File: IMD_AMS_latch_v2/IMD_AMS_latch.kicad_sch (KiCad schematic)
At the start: 40 parts, among them J10 Conn_01x02, J11 Conn_01x02, J12 Conn_01x02, J2 Conn_01x02, J5 Conn_01x02, J6 Conn_01x02, J7 Conn_01x02, J8 Conn_01x02, J9 Conn_01x02, K1 SANYOU_SRD_Form_C, K2 SANYOU_SRD_Form_C, Q1 AO3400A, Q2 AO3400A, U1 MC14044BDR2G, U2 LM393

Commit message: added TS indicator
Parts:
- removed J11, J12: Conn_01x02, Connector_Molex:Molex_Micro-Fit_3.0_43650-0215_1x02_P3.00mm_Vertical, symbol Connector_Generic:Conn_01x02
- added D5, D6: LED, LED_SMD:LED_0805_2012Metric_Pad1.15x1.40mm_HandSolder, symbol Device:LED
- added J13: Conn_01x02, Connector_Molex:Molex_Micro-Fit_3.0_43650-0215_1x02_P3.00mm_Vertical, symbol Connector_Generic:Conn_01x02
- added R16, R17: R_US, Resistor_SMD:R_0805_2012Metric_Pad1.20x1.40mm_HandSolder, symbol Device:R_US
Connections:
- net +12V: now also R16.2, R17.2
- net GND: now also J13.2 (Pin_2)
- net at D1.2 (A), K1.5, Q1.3 (D): now also D5.1 (K)
- net at D4.2 (A), R10.2: now also J13.1 (Pin_1)
- net at D2.2 (A), K2.5, Q2.3 (D): now also D6.1 (K)
- new net: D5.2 (A), R16.1
- new net: D6.2 (A), R17.1
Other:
- note added: "external IMD led"

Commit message: changed to horizontal molex microfit
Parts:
- J10, J13, J2, J5, J6, J7, J8, J9: footprint Connector_Molex:Molex_Micro-Fit_3.0_43650-0215_1x02_P3.00mm_Vertical -> Connector_Molex:Molex_Micro-Fit_3.0_43650-0200_1x02_P3.00mm_Horizontal
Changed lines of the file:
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@@
 			)
 		)
-		(property "Footprint" "Connector_Molex:Molex_Micro-Fit_3.0_43650-0215_1x02_P3.00mm_Vertical"
+		(property "Footprint" "Connector_Molex:Molex_Micro-Fit_3.0_43650-0200_1x02_P3.00mm_Horizontal"
 			(at 182.88 135.89 0)
 			(effects
@@
 			)
 		)
-		(property "Footprint" "Connector_Molex:Molex_Micro-Fit_3.0_43650-0215_1x02_P3.00mm_Vertical"
+		(property "Footprint" "Connector_Molex:Molex_Micro-Fit_3.0_43650-0200_1x02_P3.00mm_Horizontal"
 			(at 256.54 147.32 0)
 			(effects
@@
 			)
 		)
-		(property "Footprint" "Connector_Molex:Molex_Micro-Fit_3.0_43650-0215_1x02_P3.00mm_Vertical"
+		(property "Footprint" "Connector_Molex:Molex_Micro-Fit_3.0_43650-0200_1x02_P3.00mm_Horizontal"
 			(at 64.77 128.27 0)
 			(effects
@@
 			)
 		)
-		(property "Footprint" "Connector_Molex:Molex_Micro-Fit_3.0_43650-0215_1x02_P3.00mm_Vertical"
+		(property "Footprint" "Connector_Molex:Molex_Micro-Fit_3.0_43650-0200_1x02_P3.00mm_Horizontal"
 			(at 213.36 132.08 0)
 			(effects
@@
 			)
 		)
-		(property "Footprint" "Connector_Molex:Molex_Micro-Fit_3.0_43650-0215_1x02_P3.00mm_Vertical"
+		(property "Footprint" "Connector_Molex:Molex_Micro-Fit_3.0_43650-0200_1x02_P3.00mm_Horizontal"
 			(at 57.15 152.4 0)
 			(effects
@@
 			)
 		)
-		(property "Footprint" "Connector_Molex:Molex_Micro-Fit_3.0_43650-0215_1x02_P3.00mm_Vertical"
+		(property "Footprint" "Connector_Molex:Molex_Micro-Fit_3.0_43650-0200_1x02_P3.00mm_Horizontal"
 			(at 60.96 175.26 0)
 			(effects
@@
 			)
 		)
-		(property "Footprint" "Connector_Molex:Molex_Micro-Fit_3.0_43650-0215_1x02_P3.00mm_Vertical"
+		(property "Footprint" "Connector_Molex:Molex_Micro-Fit_3.0_43650-0200_1x02_P3.00mm_Horizontal"
 			(at 158.75 148.59 0)
 			(effects
@@
 			)
 		)
-		(property "Footprint" "Connector_Molex:Molex_Micro-Fit_3.0_43650-0215_1x02_P3.00mm_Vertical"
+		(property "Footprint" "Connector_Molex:Molex_Micro-Fit_3.0_43650-0200_1x02_P3.00mm_Horizontal"
 			(at 57.15 147.32 0)
 			(effects

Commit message: minor update on SDC IN & SDC out wiring
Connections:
- net SDC_IN: now also J7.2 (Pin_2); no longer J7.1 (Pin_1)
- net SDC_OUT: now also J7.1 (Pin_1); no longer J7.2 (Pin_2)
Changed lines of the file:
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@@
+	(wire
+		(pts
+			(xy 39.37 175.26) (xy 55.88 175.26)
+		)
+		(stroke
+			(width 0)
+			(type default)
+		)
+	)
 	(wire
 		(pts
@@
 	(wire
 		(pts
-			(xy 45.72 177.8) (xy 55.88 177.8)
-		)
-		(stroke
-			(width 0)
-			(type default)
-		)
-	)
-	(wire
-		(pts
 			(xy 186.69 53.34) (xy 193.04 53.34)
 		)
@@
 	(wire
 		(pts
+			(xy 39.37 177.8) (xy 55.88 177.8)
+		)
+		(stroke
+			(width 0)
+			(type default)
+		)
+	)
+	(wire
+		(pts
 			(xy 199.39 39.37) (xy 193.04 39.37)
 		)
@@
 		(pts
 			(xy 69.85 93.98) (xy 69.85 97.79)
-		)
-		(stroke
-			(width 0)
-			(type default)
-		)
-	)
-	(wire
-		(pts
-			(xy 45.72 175.26) (xy 55.88 175.26)
 		)
 		(stroke
@@
 		)
 	)
+	(label "SDC_IN"
+		(at 39.37 177.8 0)
+		(effects
+			(font
+				(size 1.27 1.27)
+			)
+			(justify left bottom)
+		)
+	)
 	(label "IMD_KL31_GND"
 		(at 194.31 134.62 0)
@@
 		)
 	)
+	(label "SDC_OUT"
+		(at 39.37 175.26 0)
+		(effects
+			(font
+				(size 1.27 1.27)
+			)
+			(justify left bottom)
+		)
+	)
 	(label "AMS_latch"
 		(at 214.63 58.42 0)
@@
 		)
 	)
-	(label "SDC_OUT"
-		(at 45.72 177.8 0)
-		(effects
-			(font
-				(size 1.27 1.27)
-			)
-			(justify left bottom)
-		)
-	)
 	(label "AMS_reset"
 		(at 87.63 38.1 0)
@@
 		(effects
 			(font
-				(size 1.27 1.27)
-			)
-			(justify left bottom)
-		)
-	)
-	(label "SDC_IN"
-		(at 45.72 175.26 0)
-		(effects
-			(font

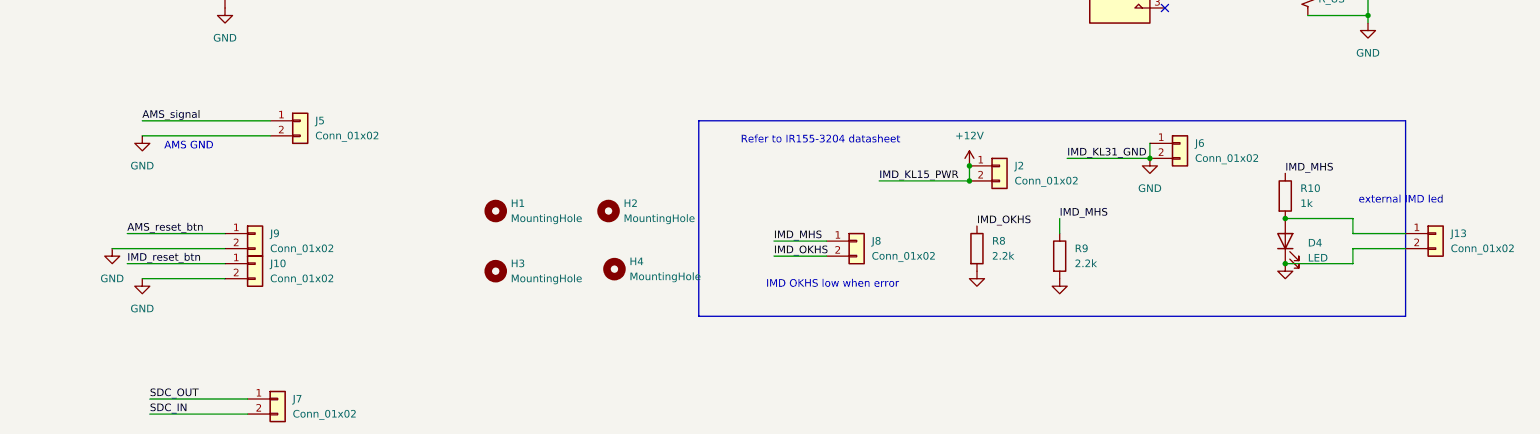
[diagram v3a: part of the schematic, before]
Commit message: fixed connectors
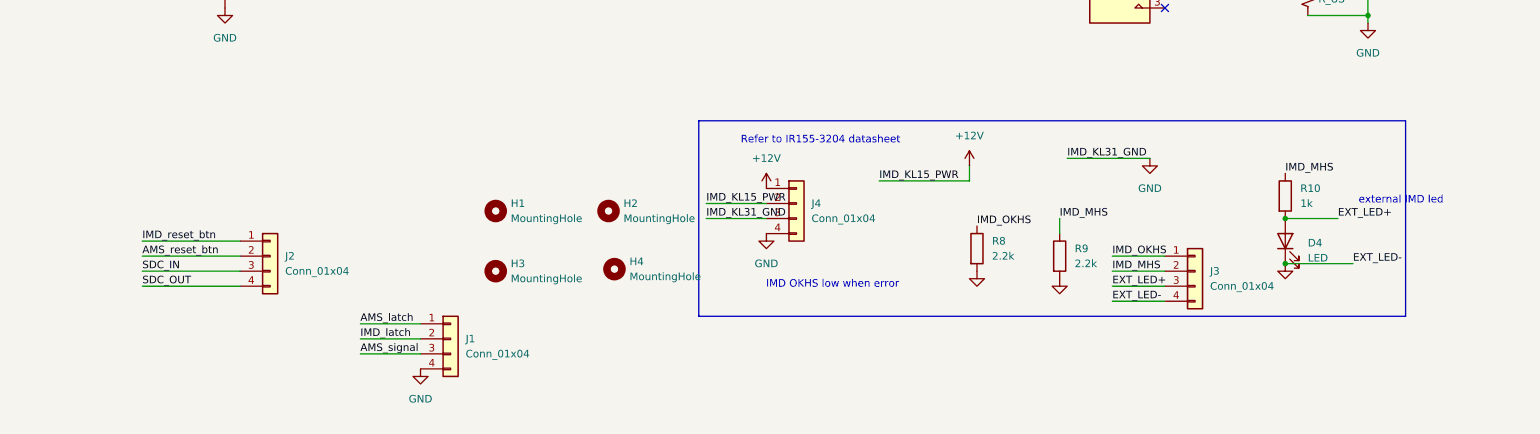
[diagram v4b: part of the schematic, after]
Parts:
- removed J10, J13, J2, J5, J6, J7, J8, J9: Conn_01x02, Connector_Molex:Molex_Micro-Fit_3.0_43650-0200_1x02_P3.00mm_Horizontal, symbol Connector_Generic:Conn_01x02
- added J1, J2, J3, J4: Conn_01x04, Connector_Molex:Molex_Micro-Fit_3.0_43045-0400_2x02_P3.00mm_Horizontal, symbol Connector_Generic:Conn_01x04
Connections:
- net +12V: now also J4.1 (Pin_1), J4.2 (Pin_2)
- net AMS_latch: now also J1.1 (Pin_1)
- net AMS_reset_btn: now also J2.2 (Pin_2)
- net AMS_signal: now also J1.3 (Pin_3)
- net GND: now also J1.4 (Pin_4), J3.4 (Pin_4), J4.3 (Pin_3), J4.4 (Pin_4)
- net IMD_MHS: now also J3.2 (Pin_2)
- net IMD_OKHS: now also J3.1 (Pin_1)
- net IMD_latch: now also J1.2 (Pin_2)
- net IMD_reset_btn: now also J2.1 (Pin_1)
- net SDC_IN: now also J2.3 (Pin_3)
- net SDC_OUT: now also J2.4 (Pin_4)
- net EXT_LED+: now reaches D4.2 (A), R10.2
- net EXT_LED+: now also J3.3 (Pin_3)
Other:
- note removed: "AMS GND"

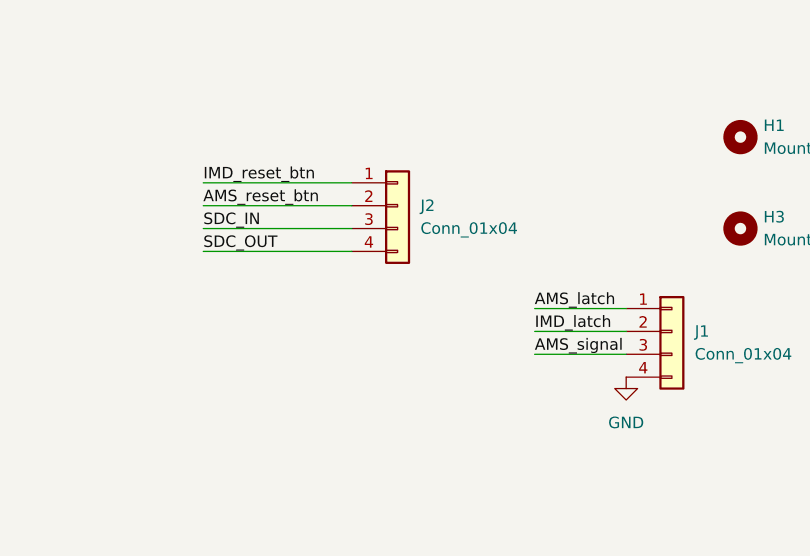
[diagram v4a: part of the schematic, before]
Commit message: fixed connectors
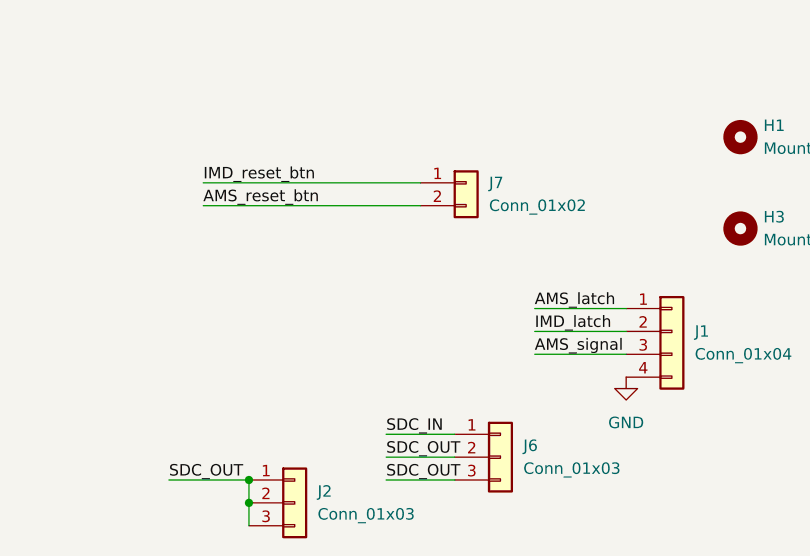
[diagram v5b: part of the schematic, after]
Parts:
- removed J2: Conn_01x04, Connector_Molex:Molex_Micro-Fit_3.0_43045-0400_2x02_P3.00mm_Horizontal, symbol Connector_Generic:Conn_01x04
- added J2, J6: Conn_01x03, Connector_Molex:Molex_Micro-Fit_3.0_43650-0300_1x03_P3.00mm_Horizontal, symbol Connector_Generic:Conn_01x03
- added J7: Conn_01x02, Connector_Molex:Molex_Micro-Fit_3.0_43650-0200_1x02_P3.00mm_Horizontal, symbol Connector_Generic:Conn_01x02
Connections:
- net AMS_reset_btn: now also J7.2 (Pin_2)
- net IMD_reset_btn: now also J7.1 (Pin_1)
- net SDC_IN: now also J6.1 (Pin_1)
- net SDC_OUT: now also J2.1 (Pin_1), J2.2 (Pin_2), J2.3 (Pin_3), J6.2 (Pin_2), J6.3 (Pin_3)
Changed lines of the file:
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@@
 	)
 	(junction
+		(at 43.18 184.15)
+		(diameter 0)
+		(color 0 0 0 0)
+	)
+	(junction
 		(at 215.9 96.52)
 		(diameter 0)
@@
 		(color 0 0 0 0)
 	)
+	(junction
+		(at 43.18 181.61)
+		(diameter 0)
+		(color 0 0 0 0)
+	)
 	(no_connect
 		(at 147.32 81.28)
@@
 	(wire
 		(pts
-			(xy 38.1 148.59) (xy 54.61 148.59)
+			(xy 38.1 148.59) (xy 62.23 148.59)
 		)
 		(stroke
@@
 	(wire
 		(pts
-			(xy 245.11 68.58) (xy 245.11 67.31)
+			(xy 58.42 181.61) (xy 66.04 181.61)
 		)
 		(stroke
@@
 	(wire
 		(pts
-			(xy 186.69 63.5) (xy 195.58 63.5)
+			(xy 245.11 68.58) (xy 245.11 67.31)
 		)
 		(stroke
@@
 	(wire
 		(pts
-			(xy 19.05 25.4) (xy 30.48 25.4)
+			(xy 186.69 63.5) (xy 195.58 63.5)
 		)
 		(stroke
@@
 	(wire
 		(pts
-			(xy 52.07 60.96) (xy 57.15 60.96)
+			(xy 19.05 25.4) (xy 30.48 25.4)
 		)
 		(stroke
@@
 	(wire
 		(pts
-			(xy 201.93 151.13) (xy 210.82 151.13)
+			(xy 52.07 60.96) (xy 57.15 60.96)
 		)
 		(stroke
@@
 	(wire
 		(pts
-			(xy 177.8 74.93) (xy 224.79 74.93)
+			(xy 201.93 151.13) (xy 210.82 151.13)
 		)
 		(stroke
@@
 	(wire
 		(pts
-			(xy 162.56 138.43) (xy 177.8 138.43)
+			(xy 177.8 74.93) (xy 224.79 74.93)
 		)
 		(stroke
@@
 	(wire
 		(pts
-			(xy 38.1 153.67) (xy 54.61 153.67)
+			(xy 162.56 138.43) (xy 177.8 138.43)
 		)
 		(stroke
@@
 	(wire
 		(pts
-			(xy 38.1 151.13) (xy 54.61 151.13)
+			(xy 43.18 181.61) (xy 43.18 184.15)
+		)
+		(stroke
+			(width 0)
+			(type default)
+		)
+	)
+	(wire
+		(pts
+			(xy 38.1 151.13) (xy 62.23 151.13)
 		)
 		(stroke
@@
 	(wire
 		(pts
+			(xy 58.42 176.53) (xy 66.04 176.53)
+		)
+		(stroke
+			(width 0)
+			(type default)
+		)
+	)
+	(wire
+		(pts
 			(xy 234.95 102.87) (xy 234.95 101.6)
 		)
@@
 	(wire
 		(pts
-			(xy 38.1 156.21) (xy 54.61 156.21)
+			(xy 199.39 39.37) (xy 193.04 39.37)
 		)
 		(stroke
@@
 	(wire
 		(pts
-			(xy 199.39 39.37) (xy 193.04 39.37)
+			(xy 40.64 76.2) (xy 40.64 74.93)
 		)
 		(stroke
@@
 	(wire
 		(pts
-			(xy 40.64 76.2) (xy 40.64 74.93)
+			(xy 69.85 93.98) (xy 69.85 97.79)
 		)
 		(stroke
@@
 	(wire
 		(pts
-			(xy 69.85 93.98) (xy 69.85 97.79)
+			(xy 147.32 35.56) (xy 147.32 36.83)
 		)
 		(stroke
@@
 	(wire
 		(pts
-			(xy 147.32 35.56) (xy 147.32 36.83)
+			(xy 43.18 184.15) (xy 43.18 186.69)
 		)
 		(stroke
@@
 	(wire
 		(pts
+			(xy 58.42 179.07) (xy 66.04 179.07)
+		)
+		(stroke
+			(width 0)
+			(type default)
+		)
+	)
+	(wire
+		(pts
 			(xy 234.95 101.6) (xy 237.49 101.6)
 		)
@@
 	(wire
 		(pts
+			(xy 34.29 181.61) (xy 43.18 181.61)
+		)
+		(stroke
+			(width 0)
+			(type default)
+		)
+	)
+	(wire
+		(pts
 			(xy 231.14 152.4) (xy 242.57 152.4)
 		)
@@
 		)
 	)
-	(label "SDC_OUT"
-		(at 38.1 156.21 0)
-		(effects
-			(font
-				(size 1.27 1.27)
-			)
-			(justify left bottom)
-		)
-	)
 	(label "IMD_MHS"
 		(at 201.93 153.67 0)
@@
 		)
 	)
+	(label "SDC_OUT"
+		(at 58.42 181.61 0)
+		(effects
+			(font
+				(size 1.27 1.27)
+			)
+			(justify left bottom)
+		)
+	)
 	(label "IMD_MHS"
 		(at 193.04 144.78 0)
@@
 		)
 	)
-	(label "IMD_latch"
-		(at 218.44 101.6 0)
+	(label "SDC_OUT"
+		(at 34.29 181.61 0)
 		(effects
 			(font
@@
 		)
 	)
-	(label "SDC_IN"
-		(at 38.1 153.67 0)
+	(label "IMD_latch"
+		(at 218.44 101.6 0)
 		(effects
 			(font
@@
 		)
 	)
+	(label "SDC_IN"
+		(at 58.42 176.53 0)
+		(effects
+			(font
+				(size 1.27 1.27)
+			)
+			(justify left bottom)
+		)
+	)
 	(label "AMS_reset_btn"
 		(at 38.1 151.13 0)
@@
 		)
 	)
+	(label "SDC_OUT"
+		(at 58.42 179.07 0)
+		(effects
+			(font
+				(size 1.27 1.27)
+			)
+			(justify left bottom)
+		)
+	)
 	(symbol
 		(lib_id "Device:R_US")
@@
 	)
 	(symbol
+		(lib_id "Connector_Generic:Conn_01x02")
+		(at 67.31 148.59 0)
+		(unit 1)
+		(exclude_from_sim no)
+		(in_bom yes)
+		(on_board yes)
+		(dnp no)
+		(fields_autoplaced yes)
+		(property "Reference" "J7"
+			(at 69.85 148.5899 0)
+			(effects
+				(font
+					(size 1.27 1.27)
+				)
+				(justify left)
+			)
+		)
+		(property "Value" "Conn_01x02"
+			(at 69.85 151.1299 0)
+			(effects
+				(font
+					(size 1.27 1.27)
+				)
+				(justify left)
+			)
+		)
+		(property "Footprint" "Connector_Molex:Molex_Micro-Fit_3.0_43650-0200_1x02_P3.00mm_Horizontal"
+			(at 67.31 148.59 0)
+			(effects
+				(font
+					(size 1.27 1.27)
+				)
+				(hide yes)
+			)
+		)
+		(property "Datasheet" "~"
+			(at 67.31 148.59 0)
+			(effects
+				(font
+					(size 1.27 1.27)
+				)
+				(hide yes)
+			)
+		)
+		(property "Description" "Generic connector, single row, 01x02, script generated (kicad-library-utils/schlib/autogen/connector/)"
+			(at 67.31 148.59 0)
+			(effects
+				(font
+					(size 1.27 1.27)
+				)
+				(hide yes)
+			)
+		)
+		(pin "1"
+		)
+		(pin "2"
+		)
+		(instances
+			(project "IMD_AMS_latch"
+				(path "/5826de07-2dfc-4b26-8f2d-f37e9b29b777"
+					(reference "J7")
+					(unit 1)
+				)
+			)
+		)
+	)
+	(symbol
 		(lib_id "power:GND")
 		(at 193.04 154.94 0)
@@
 	)
 	(symbol
-		(lib_id "Connector_Generic:Conn_01x04")
-		(at 59.69 151.13 0)
+		(lib_id "Connector_Generic:Conn_01x03")
+		(at 48.26 184.15 0)
 		(unit 1)
 		(exclude_from_sim no)
@@
 		(fields_autoplaced yes)
 		(property "Reference" "J2"
-			(at 62.23 151.1299 0)
+			(at 50.8 182.8799 0)
 			(effects
 				(font
@@
 			)
 		)
-		(property "Value" "Conn_01x04"
-			(at 62.23 153.6699 0)
+		(property "Value" "Conn_01x03"
+			(at 50.8 185.4199 0)
 			(effects
 				(font
@@
 			)
 		)
-		(property "Footprint" "Connector_Molex:Molex_Micro-Fit_3.0_43045-0400_2x02_P3.00mm_Horizontal"
-			(at 59.69 151.13 0)
+		(property "Footprint" "Connector_Molex:Molex_Micro-Fit_3.0_43650-0300_1x03_P3.00mm_Horizontal"
+			(at 48.26 184.15 0)
 			(effects
 				(font
@@
 		)
 		(property "Datasheet" "~"
-			(at 59.69 151.13 0)
+			(at 48.26 184.15 0)
 			(effects
 				(font
@@
 			)
 		)
-		(property "Description" "Generic connector, single row, 01x04, script generated (kicad-library-utils/schlib/autogen/connector/)"
-			(at 59.69 151.13 0)
+		(property "Description" "Generic connector, single row, 01x03, script generated (kicad-library-utils/schlib/autogen/connector/)"
+			(at 48.26 184.15 0)
 			(effects
 				(font
@@
 		(pin "1"
 		)
-		(pin "3"
-		)
-		(pin "4"
-		)
 		(pin "2"
 		)
+		(pin "3"
+		)
 		(instances
-			(project "IMD_AMS_latch"
+			(project ""
 				(path "/5826de07-2dfc-4b26-8f2d-f37e9b29b777"
 					(reference "J2")
@@
 					(unit 1)
 				)
+			)
+		)
+	)
+	(symbol
+		(lib_id "Connector_Generic:Conn_01x03")
+		(at 71.12 179.07 0)
+		(unit 1)
+		(exclude_from_sim no)
+		(in_bom yes)
+		(on_board yes)
+		(dnp no)
+		(fields_autoplaced yes)
+		(property "Reference" "J6"
+			(at 73.66 177.7999 0)
+			(effects
+				(font
+					(size 1.27 1.27)
+				)
+				(justify left)
+			)
+		)
+		(property "Value" "Conn_01x03"
+			(at 73.66 180.3399 0)
+			(effects
+				(font
+					(size 1.27 1.27)
+				)
+				(justify left)
+			)
+		)
+		(property "Footprint" "Connector_Molex:Molex_Micro-Fit_3.0_43650-0300_1x03_P3.00mm_Horizontal"
+			(at 71.12 179.07 0)
+			(effects
+				(font
+					(size 1.27 1.27)
+				)
+				(hide yes)
+			)
+		)
+		(property "Datasheet" "~"
+			(at 71.12 179.07 0)
+			(effects
+				(font
+					(size 1.27 1.27)
+				)
+				(hide yes)
+			)
+		)
+		(property "Description" "Generic connector, single row, 01x03, script generated (kicad-library-utils/schlib/autogen/connector/)"
+			(at 71.12 179.07 0)
+			(effects
+				(font
+					(size 1.27 1.27)
+				)
+				(hide yes)
+			)
+		)
+		(pin "1"
+		)
+		(pin "2"
+		)
+		(pin "3"
+		)
+		(instances
+			(project "IMD_AMS_latch"
+				(path "/5826de07-2dfc-4b26-8f2d-f37e9b29b777"
+					(reference "J6")
+					(unit 1)
+				)
